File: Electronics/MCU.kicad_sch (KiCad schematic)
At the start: 7 parts, among them U301 74HC86, U302 74AHC08

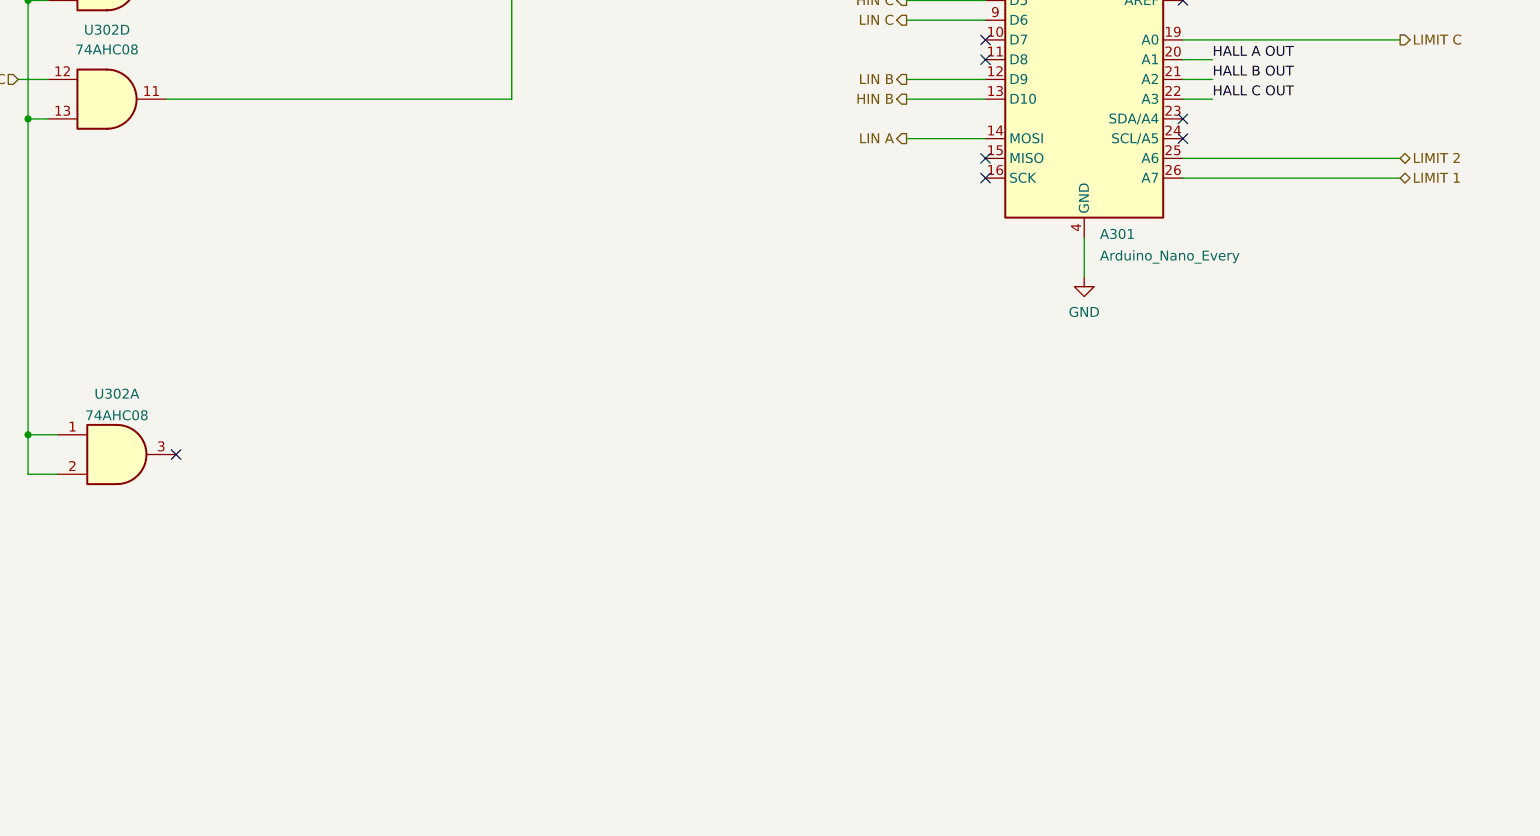
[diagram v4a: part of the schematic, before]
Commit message: Added current sensor circuitry
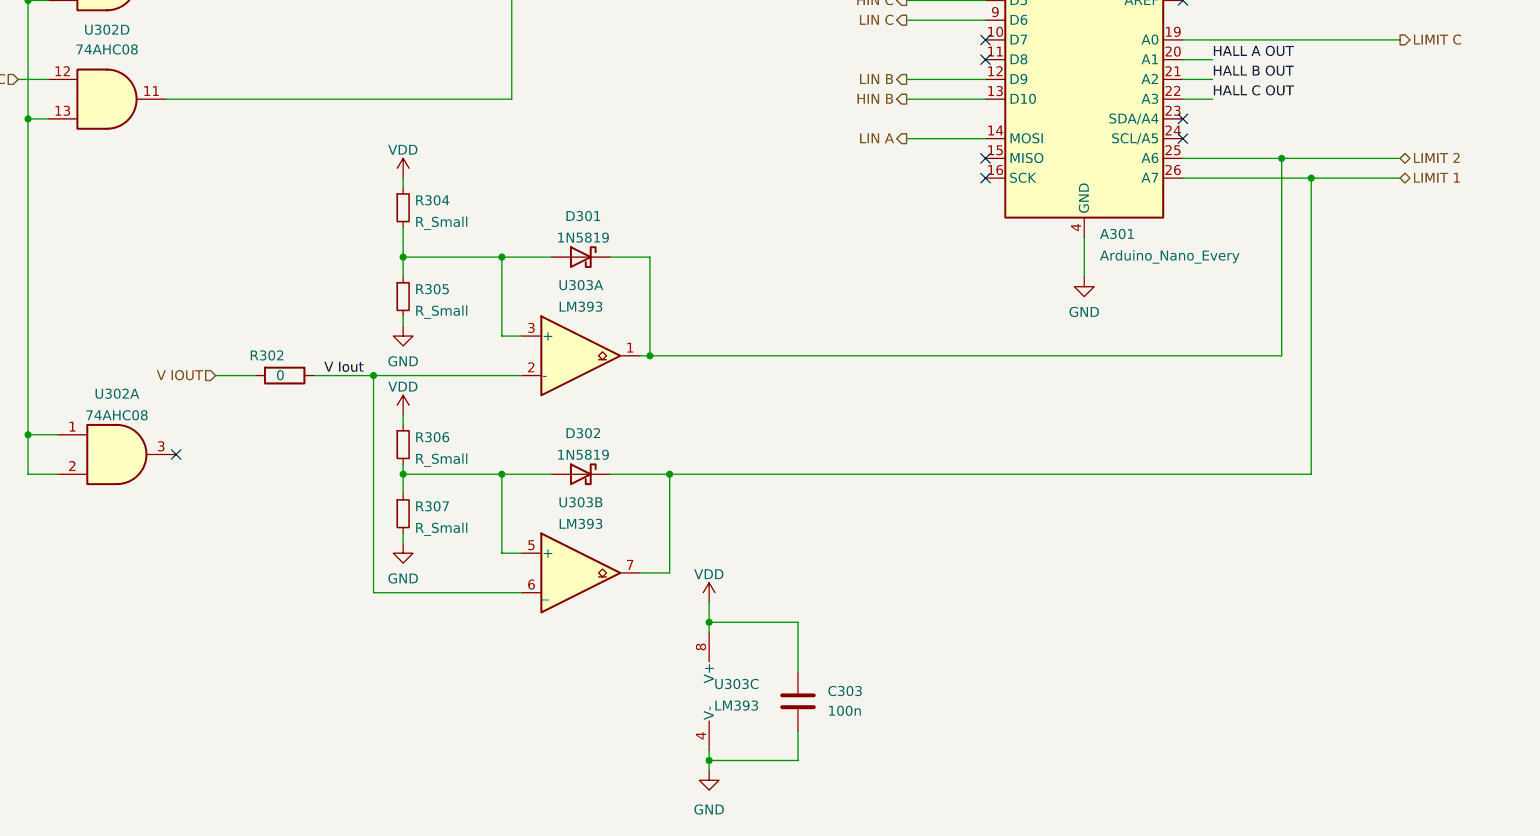
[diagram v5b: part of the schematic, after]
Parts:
- added C303: 100n, Capacitor_SMD:C_0603_1608Metric_Pad1.08x0.95mm_HandSolder, symbol Device:C
- added D301, D302: 1N5819, Diode_SMD:D_SOD-123, symbol Diode:1N5819
- added R302: 0, Resistor_SMD:R_0603_1608Metric_Pad0.98x0.95mm_HandSolder, symbol Device:R
- added R304, R305, R306, R307: R_Small, Resistor_SMD:R_0603_1608Metric_Pad0.98x0.95mm_HandSolder, symbol Device:R_Small
- added U303: LM393, Package_SO:SO-8_3.9x4.9mm_P1.27mm, symbol Comparator:LM393
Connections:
- net GND: now also C303.1, R305.2, R307.2, U303.4 (V-)
- net LIMIT 1: now also D302.1 (K), U303.7
- net LIMIT 2: now also D301.1 (K), U303.1
- net VDD: now also C303.2, R304.1, R306.1, U303.8 (V+)
- new net: D302.2 (A), R306.2, R307.1, U303.5 (+)
- new net: D301.2 (A), R304.2, R305.1, U303.3 (+)
- new net V IOUT: R302.2
- new net V Iout: R302.1, U303.2 (-), U303.6 (_)

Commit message: Updated Design
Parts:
- removed D301, D302: 1N5819, Diode_SMD:D_SOD-123, symbol Diode:1N5819
- removed R304, R305, R306, R307: R_Small, Resistor_SMD:R_0603_1608Metric_Pad0.98x0.95mm_HandSolder, symbol Device:R_Small
- removed U303: LM393, Package_SO:SO-8_3.9x4.9mm_P1.27mm, symbol Comparator:LM393
- added J301: UART, Connector_PinHeader_2.54mm:PinHeader_1x03_P2.54mm_Vertical, symbol Connector_Generic:Conn_01x03
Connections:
- net V Iout is gone; now on an unnamed net: R302.1
- net +3V3: now also R302.2
- net GND: now also J301.2 (Pin_2)
- net LIMIT 1: now also A301.10 (D7); no longer A301.26 (A7)
- net LIMIT 2: now also A301.11 (D8); no longer A301.25 (A6)
- net LIMIT C: now also A301.15 (MISO); no longer A301.19 (A0)
- net V IOUT: now also A301.25 (A6); no longer R302.2
- net VDD: no longer C303.2, U302.1, U302.2
- net TX: now reaches A301.1 (TX1)
- net TX: now also J301.3 (Pin_3)
- net at A301.18 (AREF): now also C303.2
- net RX: now reaches A301.2 (RX1)
- net RX: now also J301.1 (Pin_1)
- net Latch Reset: now reaches A301.7 (D4)
- no-connect marks 15 -> 7
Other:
- moved on the sheet: U302A

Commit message: Chaned 74AHC08 footprint to ssop-14
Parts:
- U302: footprint Package_SO:SO-14_3.9x8.65mm_P1.27mm -> Package_SO:SSOP-14_5.3x6.2mm_P0.65mm
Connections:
- net +3V3: now also U302.10, U302.13, U302.5
- net VDD: no longer U302.10, U302.13, U302.5
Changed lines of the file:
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@@
+    (pin "1")
+  )
+  (symbol (lib_id "power:+3V3") (at 27.94 62.23 0) (unit 1)
+    (in_bom yes) (on_board yes) (fields_autoplaced)
+    (property "Reference" "#PWR?" (id 0) (at 27.94 66.04 0)
+      (effects (font (size 1.27 1.27)) hide)
+    )
+    (property "Value" "+3V3" (id 1) (at 27.94 57.15 0))
+    (property "Footprint" "" (id 2) (at 27.94 62.23 0)
+      (effects (font (size 1.27 1.27)) hide)
+    )
+    (property "Datasheet" "" (id 3) (at 27.94 62.23 0)
+      (effects (font (size 1.27 1.27)) hide)
+    )
     (pin "1")
   )
@@
     (property "Reference" "U302" (id 0) (at 38.1 78.74 0))
     (property "Value" "74AHC08" (id 1) (at 38.1 81.28 0))
-    (property "Footprint" "Package_SO:SO-14_3.9x8.65mm_P1.27mm" (id 2) (at 38.1 87.63 0)
+    (property "Footprint" "Package_SO:SSOP-14_5.3x6.2mm_P0.65mm" (id 2) (at 38.1 87.63 0)
       (effects (font (size 1.27 1.27)) hide)
     )
@@
     (property "Reference" "U302" (id 0) (at 38.1 93.98 0))
     (property "Value" "74AHC08" (id 1) (at 38.1 96.52 0))
-    (property "Footprint" "Package_SO:SO-14_3.9x8.65mm_P1.27mm" (id 2) (at 38.1 102.87 0)
+    (property "Footprint" "Package_SO:SSOP-14_5.3x6.2mm_P0.65mm" (id 2) (at 38.1 102.87 0)
       (effects (font (size 1.27 1.27)) hide)
     )
@@
     (property "Reference" "U302" (id 0) (at 38.1 63.5 0))
     (property "Value" "74AHC08" (id 1) (at 38.1 66.04 0))
-    (property "Footprint" "Package_SO:SO-14_3.9x8.65mm_P1.27mm" (id 2) (at 38.1 72.39 0)
+    (property "Footprint" "Package_SO:SSOP-14_5.3x6.2mm_P0.65mm" (id 2) (at 38.1 72.39 0)
       (effects (font (size 1.27 1.27)) hide)
     )
@@
       (effects (font (size 1.27 1.27)) (justify left))
     )
-    (property "Footprint" "Package_SO:SO-14_3.9x8.65mm_P1.27mm" (id 2) (at 262.89 100.33 0)
+    (property "Footprint" "Package_SO:SSOP-14_5.3x6.2mm_P0.65mm" (id 2) (at 262.89 100.33 0)
       (effects (font (size 1.27 1.27)) hide)
     )
@@
     (pin "1")
     (pin "2")
-  )
-  (symbol (lib_id "power:VDD") (at 27.94 62.23 0) (unit 1)
-    (in_bom yes) (on_board yes) (fields_autoplaced)
-    (property "Reference" "#PWR0114" (id 0) (at 27.94 66.04 0)
-      (effects (font (size 1.27 1.27)) hide)
-    )
-    (property "Value" "VDD" (id 1) (at 27.94 57.15 0))
-    (property "Footprint" "" (id 2) (at 27.94 62.23 0)
-      (effects (font (size 1.27 1.27)) hide)
-    )
-    (property "Datasheet" "" (id 3) (at 27.94 62.23 0)
-      (effects (font (size 1.27 1.27)) hide)
-    )
-    (pin "1")
   )
   (symbol (lib_id "Device:R") (at 183.515 85.725 180) (unit 1)
@@
     (property "Reference" "U302" (id 0) (at 29.21 182.7235 0))
     (property "Value" "74AHC08" (id 1) (at 29.21 185.4986 0))
-    (property "Footprint" "Package_SO:SO-14_3.9x8.65mm_P1.27mm" (id 2) (at 29.21 190.5 0)
-      (effects (font (size 1.27 1.27)) hide)
-    )
+    (property "Footprint" "Package_SO:SSOP-14_5.3x6.2mm_P0.65mm" (id 2) (at 29.21 190.5 0)
+      (effects (font (size 1.27 1.27)) hide)
+    )

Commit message: Layout improvements
Signed-off-by: Aki Kuusela <git@findersee.fi>
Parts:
- added J302: I2C, Connector_PinHeader_2.54mm:PinHeader_1x04_P2.54mm_Vertical, symbol Connector_Generic:Conn_01x04
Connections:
- net +3V3: now also J302.1 (Pin_1)
- net GND: now also U302.1, U302.2, J302.4 (Pin_4)
- net at A301.23 (SDA/A4): now also J302.2 (Pin_2)
- net at A301.24 (SCL/A5): now also J302.3 (Pin_3)
- net OCP: now reaches A301.26 (A7)
- net LIMIT 1 renamed LIMIT MCU 1
- net LIMIT 2 renamed LIMIT MCU 2
- no-connect marks 7 -> 8
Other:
- company: (none) -> findersee.fi
- title: (none) -> Motor Controller
- moved on the sheet: U302A
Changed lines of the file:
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@@
 (kicad_sch (version 20211123) (generator eeschema)
   (paper "A4")
+  (title_block
+    (title "Motor Controller")
+    (date "2022-02-18")
+    (rev "1.0")
+    (company "findersee.fi")
+  )
   (junction (at 208.28 72.39) (diameter 0) (color 0 0 0 0)
   )
@@
   (junction (at 262.89 86.36) (diameter 0) (color 0 0 0 0)
   )
+  (junction (at 19.05 187.96) (diameter 0) (color 0 0 0 0)
+  )
   (junction (at 166.37 45.72) (diameter 0) (color 0 0 0 0)
   )
@@
   (junction (at 208.28 67.31) (diameter 0) (color 0 0 0 0)
   )
+  (no_connect (at 36.83 185.42))
   (no_connect (at 151.13 113.03))
-  (no_connect (at 176.53 107.95))
-  (no_connect (at 176.53 105.41))
   (no_connect (at 176.53 80.01))
   (no_connect (at 176.53 82.55))
   (no_connect (at 227.33 55.88))
   (no_connect (at 227.33 69.85))
+  (no_connect (at 161.29 69.85))
+  (no_connect (at 176.53 95.25))
   (wire (pts (xy 262.89 19.05) (xy 262.89 21.59))
     (stroke (width 0) (type default) (color 0 0 0 0))
@@
     (stroke (width 0) (type default) (color 0 0 0 0))
   )
+  (wire (pts (xy 203.2 102.87) (xy 203.2 100.33))
+    (stroke (width 0) (type default) (color 0 0 0 0))
+  )
   (wire (pts (xy 208.28 67.31) (xy 208.28 72.39))
     (stroke (width 0) (type default) (color 0 0 0 0))
@@
     (stroke (width 0) (type default) (color 0 0 0 0))
   )
+  (wire (pts (xy 21.59 182.88) (xy 19.05 182.88))
+    (stroke (width 0) (type default) (color 0 0 0 0))
+  )
   (wire (pts (xy 176.53 90.17) (xy 183.515 90.17))
     (stroke (width 0) (type default) (color 0 0 0 0))
@@
     (stroke (width 0) (type default) (color 0 0 0 0))
   )
+  (wire (pts (xy 176.53 107.95) (xy 205.74 107.95))
+    (stroke (width 0) (type default) (color 0 0 0 0))
+  )
   (wire (pts (xy 262.89 114.3) (xy 262.89 115.57))
     (stroke (width 0) (type default) (color 0 0 0 0))
@@
     (stroke (width 0) (type default) (color 0 0 0 0))
   )
+  (wire (pts (xy 203.2 110.49) (xy 205.74 110.49))
+    (stroke (width 0) (type default) (color 0 0 0 0))
+  )
   (wire (pts (xy 176.53 110.49) (xy 187.325 110.49))
     (stroke (width 0) (type default) (color 0 0 0 0))
   )
+  (wire (pts (xy 19.05 182.88) (xy 19.05 187.96))
+    (stroke (width 0) (type default) (color 0 0 0 0))
+  )
   (wire (pts (xy 197.485 90.17) (xy 197.485 91.44))
     (stroke (width 0) (type default) (color 0 0 0 0))
@@
     (stroke (width 0) (type default) (color 0 0 0 0))
   )
+  (wire (pts (xy 187.325 113.03) (xy 176.53 113.03))
+    (stroke (width 0) (type default) (color 0 0 0 0))
+  )
   (wire (pts (xy 50.8 77.47) (xy 78.74 77.47))
     (stroke (width 0) (type default) (color 0 0 0 0))
@@
     (stroke (width 0) (type default) (color 0 0 0 0))
   )
+  (wire (pts (xy 203.2 110.49) (xy 203.2 114.3))
+    (stroke (width 0) (type default) (color 0 0 0 0))
+  )
   (wire (pts (xy 176.53 45.72) (xy 176.53 49.53))
     (stroke (width 0) (type default) (color 0 0 0 0))
   )
+  (wire (pts (xy 176.53 105.41) (xy 205.74 105.41))
+    (stroke (width 0) (type default) (color 0 0 0 0))
+  )
+  (wire (pts (xy 19.05 187.96) (xy 21.59 187.96))
+    (stroke (width 0) (type default) (color 0 0 0 0))
+  )
   (wire (pts (xy 140.97 107.95) (xy 151.13 107.95))
     (stroke (width 0) (type default) (color 0 0 0 0))
@@
     (stroke (width 0) (type default) (color 0 0 0 0))
   )
+  (wire (pts (xy 205.74 102.87) (xy 203.2 102.87))
+    (stroke (width 0) (type default) (color 0 0 0 0))
+  )
   (wire (pts (xy 26.67 100.33) (xy 30.48 100.33))
     (stroke (width 0) (type default) (color 0 0 0 0))
@@
   )
   (wire (pts (xy 262.89 50.8) (xy 262.89 52.07))
+    (stroke (width 0) (type default) (color 0 0 0 0))
+  )
+  (wire (pts (xy 19.05 187.96) (xy 19.05 191.77))
     (stroke (width 0) (type default) (color 0 0 0 0))
   )
@@
     (effects (font (size 1.27 1.27)) (justify right))
   )
-  (hierarchical_label "LIMIT 1" (shape bidirectional) (at 140.97 95.25 180)
+  (hierarchical_label "OCP" (shape input) (at 187.325 113.03 0)
+    (effects (font (size 1.27 1.27)) (justify left))
+  )
+  (hierarchical_label "LIMIT MCU 1" (shape bidirectional) (at 140.97 95.25 180)
     (effects (font (size 1.27 1.27)) (justify right))
   )
@@
     (effects (font (size 1.27 1.27)) (justify right))
   )
-  (hierarchical_label "LIMIT 2" (shape bidirectional) (at 140.97 97.79 180)
+  (hierarchical_label "LIMIT MCU 2" (shape bidirectional) (at 140.97 97.79 180)
     (effects (font (size 1.27 1.27)) (justify right))
   )
@@
   (symbol (lib_id "power:+3V3") (at 27.94 62.23 0) (unit 1)
     (in_bom yes) (on_board yes) (fields_autoplaced)
-    (property "Reference" "#PWR?" (id 0) (at 27.94 66.04 0)
+    (property "Reference" "#PWR0114" (id 0) (at 27.94 66.04 0)
       (effects (font (size 1.27 1.27)) hide)
     )
@@
     (pin "7")
   )
+  (symbol (lib_id "power:GND") (at 19.05 191.77 0) (unit 1)
+    (in_bom yes) (on_board yes) (fields_autoplaced)
+    (property "Reference" "#PWR0148" (id 0) (at 19.05 198.12 0)
+      (effects (font (size 1.27 1.27)) hide)
+    )
+    (property "Value" "GND" (id 1) (at 19.05 196.85 0))
+    (property "Footprint" "" (id 2) (at 19.05 191.77 0)
+      (effects (font (size 1.27 1.27)) hide)
+    )
+    (property "Datasheet" "" (id 3) (at 19.05 191.77 0)
+      (effects (font (size 1.27 1.27)) hide)
+    )
+    (pin "1")
+  )
   (symbol (lib_id "power:GND") (at 140.335 68.58 0) (unit 1)
     (in_bom yes) (on_board yes) (fields_autoplaced)
@@
     (pin "3")
   )
+  (symbol (lib_id "power:+3V3") (at 203.2 100.33 0) (unit 1)
+    (in_bom yes) (on_board yes) (fields_autoplaced)
+    (property "Reference" "#PWR0146" (id 0) (at 203.2 104.14 0)
+      (effects (font (size 1.27 1.27)) hide)
+    )
+    (property "Value" "+3V3" (id 1) (at 204.597 99.539 0)
+      (effects (font (size 1.27 1.27)) (justify left))
+    )
+    (property "Footprint" "" (id 2) (at 203.2 100.33 0)
+      (effects (font (size 1.27 1.27)) hide)
+    )
+    (property "Datasheet" "" (id 3) (at 203.2 100.33 0)
+      (effects (font (size 1.27 1.27)) hide)
+    )
+    (pin "1")
+  )
+  (symbol (lib_id "Connector_Generic:Conn_01x04") (at 210.82 105.41 0) (unit 1)
+    (in_bom yes) (on_board yes) (fields_autoplaced)
+    (property "Reference" "J302" (id 0) (at 213.36 105.4099 0)
+      (effects (font (size 1.27 1.27)) (justify left))
+    )
+    (property "Value" "I2C" (id 1) (at 213.36 107.9499 0)
+      (effects (font (size 1.27 1.27)) (justify left))
+    )
+    (property "Footprint" "Connector_PinHeader_2.54mm:PinHeader_1x04_P2.54mm_Vertical" (id 2) (at 210.82 105.41 0)
+      (effects (font (size 1.27 1.27)) hide)
+    )
+    (property "Datasheet" "~" (id 3) (at 210.82 105.41 0)
+      (effects (font (size 1.27 1.27)) hide)
+    )
+    (pin "1")
+    (pin "2")
+    (pin "3")
+    (pin "4")
+  )
   (symbol (lib_id "power:+3V3") (at 183.515 80.645 0) (unit 1)
     (in_bom yes) (on_board yes) (fields_autoplaced)
@@
     (pin "1")
     (pin "2")
+  )
+  (symbol (lib_id "power:GND") (at 203.2 114.3 0) (unit 1)
+    (in_bom yes) (on_board yes) (fields_autoplaced)
+    (property "Reference" "#PWR0145" (id 0) (at 203.2 120.65 0)
+      (effects (font (size 1.27 1.27)) hide)
+    )
+    (property "Value" "GND" (id 1) (at 203.2 118.8625 0))
+    (property "Footprint" "" (id 2) (at 203.2 114.3 0)
+      (effects (font (size 1.27 1.27)) hide)
+    )
+    (property "Datasheet" "" (id 3) (at 203.2 114.3 0)
+      (effects (font (size 1.27 1.27)) hide)
+    )
+    (pin "1")
   )
   (symbol (lib_id "Device:R") (at 183.515 85.725 180) (unit 1)
@@
     (pin "6")
   )
-  (symbol (lib_id "74xx:74LS08") (at 29.21 190.5 0) (unit 1)
-    (in_bom yes) (on_board yes) (fields_autoplaced)
-    (property "Reference" "U302" (id 0) (at 29.21 182.7235 0))
-    (property "Value" "74AHC08" (id 1) (at 29.21 185.4986 0))
-    (property "Footprint" "Package_SO:SSOP-14_5.3x6.2mm_P0.65mm" (id 2) (at 29.21 190.5 0)
-      (effects (font (size 1.27 1.27)) hide)
-    )
-    (property "Datasheet" "http://www.ti.com/lit/gpn/sn74LS08" (id 3) (at 29.21 190.5 0)
-      (effects (font (size 1.27 1.27)) hide)
-    )
+  (symbol (lib_id "74xx:74LS08") (at 29.21 185.42 0) (unit 1)
+    (in_bom yes) (on_board yes) (fields_autoplaced)
+    (property "Reference" "U302" (id 0) (at 29.21 177.6435 0))
+    (property "Value" "74AHC08" (id 1) (at 29.21 180.4186 0))
+    (property "Footprint" "Package_SO:SSOP-14_5.3x6.2mm_P0.65mm" (id 2) (at 29.21 185.42 0)
+      (effects (font (size 1.27 1.27)) hide)
+    )
+    (property "Datasheet" "http://www.ti.com/lit/gpn/sn74LS08" (id 3) (at 29.21 185.42 0)
+      (effects (font (size 1.27 1.27)) hide)
+    )
